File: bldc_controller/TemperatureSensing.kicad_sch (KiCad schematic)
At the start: 9 parts

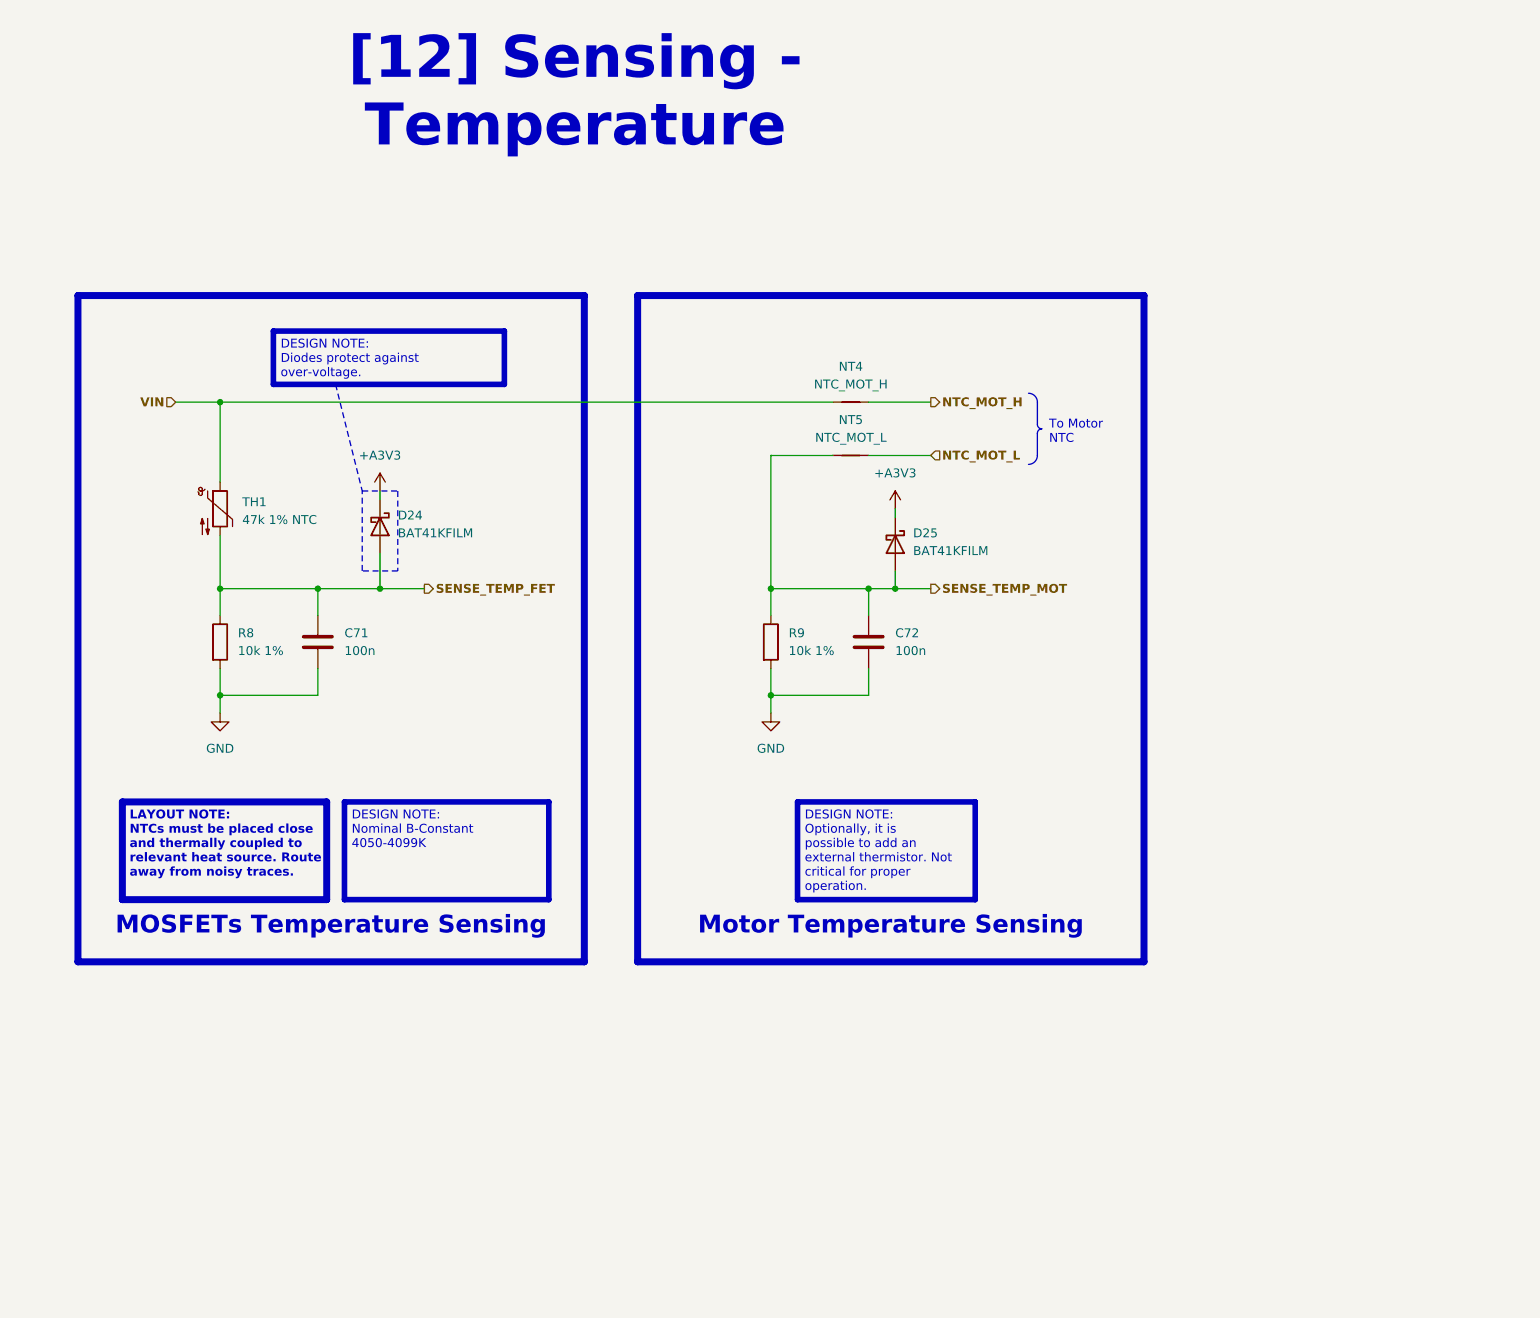
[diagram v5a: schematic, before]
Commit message: Replaced 3v3 buck with WSON package alternative. Will back-annotate components
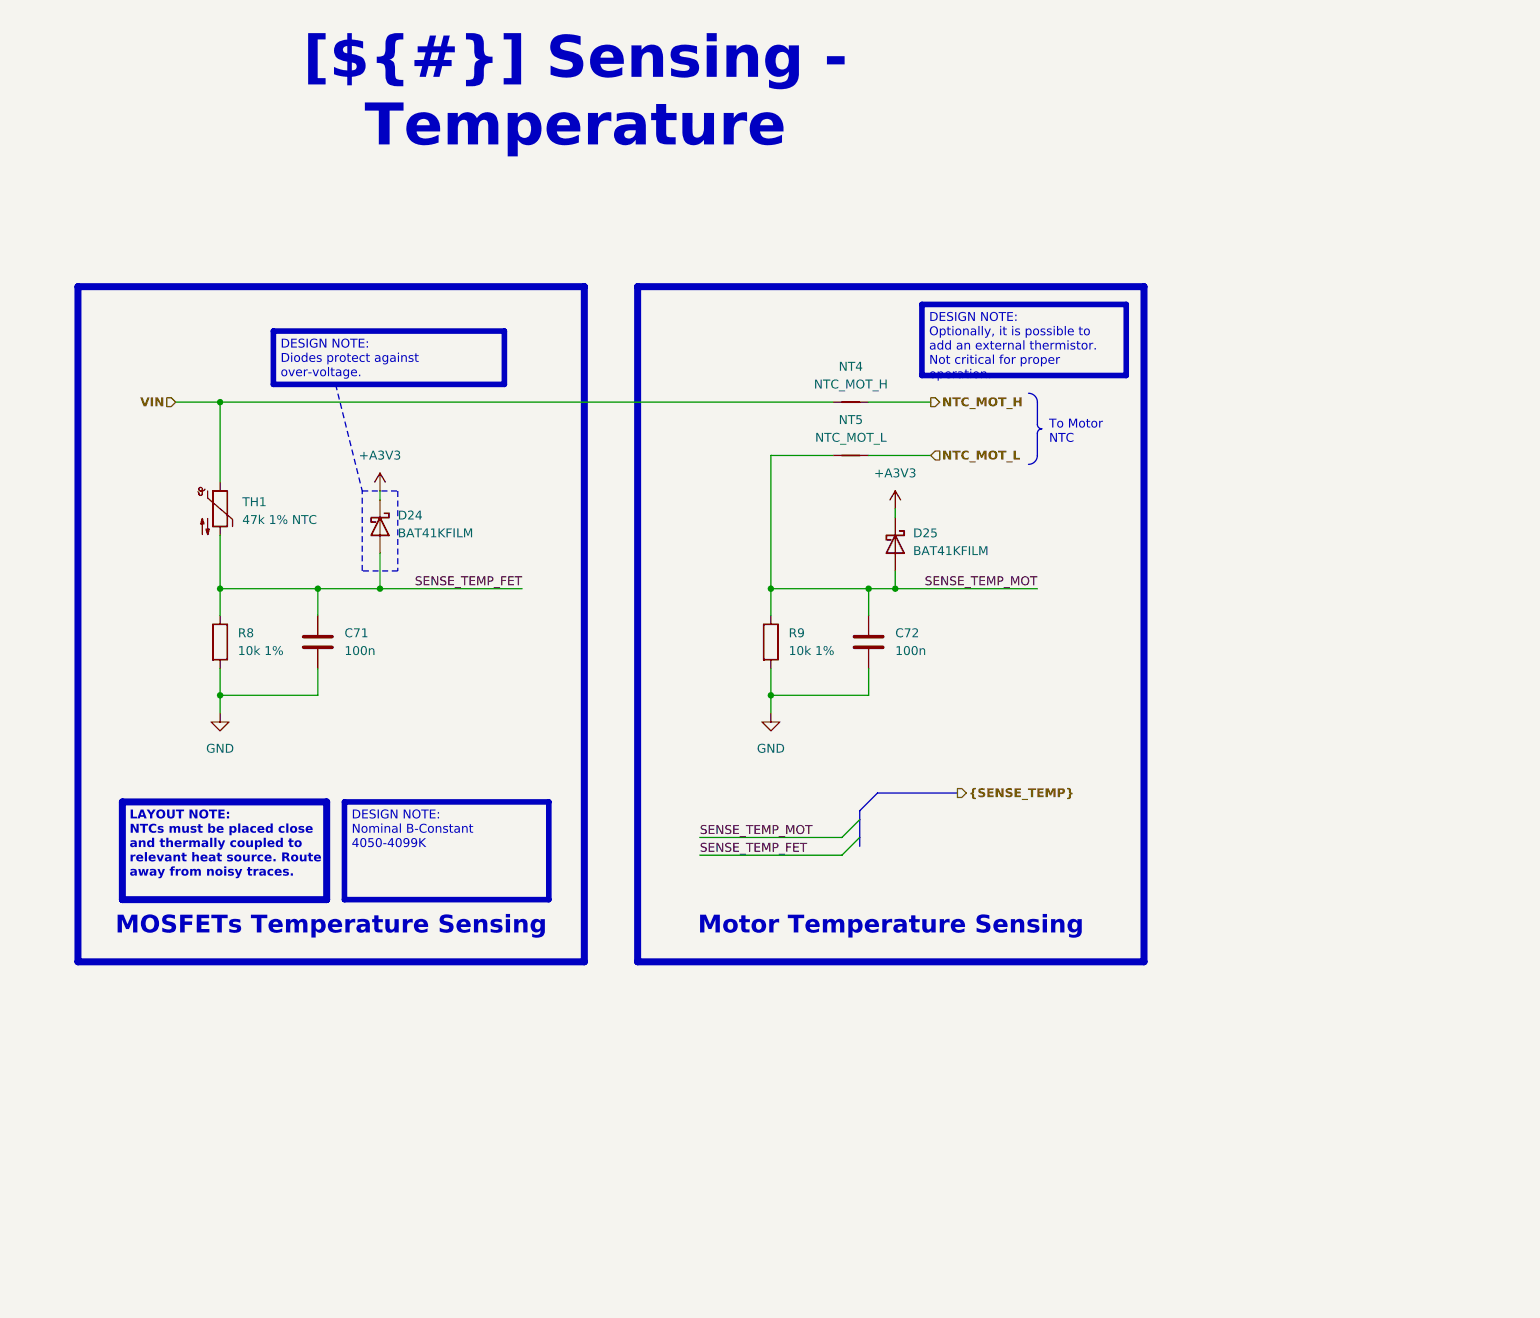
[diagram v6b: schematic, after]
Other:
- company: EPFL Xplore -> ${COMPANY}
- title: Temperature Sensing -> Sensing - Temperature
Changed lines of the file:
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@@
   (paper "A4")
   (title_block
-    (title "Temperature Sensing")
+    (title "Sensing - Temperature")
     (date "2023-10-14")
-    (rev "1.0")
-    (company "EPFL Xplore")
-    (comment 3 "Author: Vincent Nguyen")
+    (rev "${REVISION}")
+    (company "${COMPANY}")
+    (comment 3 "Author: ${AUTHOR}")
   )
   (junction (at 194.31 93.98) (diameter 0) (color 0 0 0 0)
@@
   (junction (at 190.5 93.98) (diameter 0) (color 0 0 0 0)
   )
-  (junction (at 97.79 109.22) (diameter 0) (color 0 0 0 1)
-  )
-  (junction (at 176.53 109.22) (diameter 0) (color 0 0 0 1)
+  (junction (at 97.79 109.22) (diameter 0) (color 0 0 0 0)
+  )
+  (junction (at 176.53 109.22) (diameter 0) (color 0 0 0 0)
   )
   (junction (at 111.76 93.98) (diameter 0) (color 0 0 0 0)
   )
+  (bus_entry (at 186.69 129.54) (size 2.54 -2.54)
+    (stroke (width 0) (type default))
+  )
+  (bus_entry (at 186.69 132.08) (size 2.54 -2.54)
+    (stroke (width 0) (type default))
+  )
   (wire (pts (xy 97.79 67.31) (xy 185.42 67.31))
     (stroke (width 0) (type default))
@@
   )
   (wire (pts (xy 176.53 109.22) (xy 190.5 109.22))
-    (stroke (width 0.381) (type default) (color 0 0 0 1))
+    (stroke (width 0) (type default))
   )
   (wire (pts (xy 120.65 80.01) (xy 120.65 81.28))
@@
   )
   (wire (pts (xy 97.79 109.22) (xy 111.76 109.22))
-    (stroke (width 0.381) (type default) (color 0 0 0 1))
+    (stroke (width 0) (type default))
   )
   (wire (pts (xy 97.79 93.98) (xy 97.79 97.79))
@@
   )
   (wire (pts (xy 97.79 105.41) (xy 97.79 109.22))
-    (stroke (width 0.381) (type default) (color 0 0 0 1))
+    (stroke (width 0) (type default))
   )
   (wire (pts (xy 97.79 111.76) (xy 97.79 109.22))
-    (stroke (width 0.381) (type default) (color 0 0 0 1))
+    (stroke (width 0) (type default))
   )
   (wire (pts (xy 111.76 93.98) (xy 120.65 93.98))
@@
   )
   (wire (pts (xy 190.5 105.41) (xy 190.5 109.22))
-    (stroke (width 0.381) (type default) (color 0 0 0 1))
+    (stroke (width 0) (type default))
   )
   (wire (pts (xy 111.76 93.98) (xy 111.76 97.79))
     (stroke (width 0) (type default))
   )
-  (wire (pts (xy 120.65 93.98) (xy 127 93.98))
+  (bus (pts (xy 191.77 123.19) (xy 203.2 123.19))
+    (stroke (width 0) (type default))
+  )
+  (wire (pts (xy 120.65 93.98) (xy 140.97 93.98))
     (stroke (width 0) (type default))
   )
@@
     (stroke (width 0) (type default))
   )
+  (bus (pts (xy 189.23 127) (xy 189.23 129.54))
+    (stroke (width 0) (type default))
+  )
+  (bus (pts (xy 189.23 129.54) (xy 189.23 130.81))
+    (stroke (width 0) (type default))
+  )
   (wire (pts (xy 194.31 91.44) (xy 194.31 93.98))
     (stroke (width 0) (type default))
@@
     (stroke (width 0) (type default))
   )
+  (bus (pts (xy 189.23 125.73) (xy 191.77 123.19))
+    (stroke (width 0) (type default))
+  )
   (wire (pts (xy 176.53 111.76) (xy 176.53 109.22))
-    (stroke (width 0.381) (type default) (color 0 0 0 1))
+    (stroke (width 0) (type default))
   )
   (wire (pts (xy 190.5 93.98) (xy 190.5 97.79))
@@
   )
   (wire (pts (xy 111.76 105.41) (xy 111.76 109.22))
-    (stroke (width 0.381) (type default) (color 0 0 0 1))
-  )
-  (wire (pts (xy 194.31 93.98) (xy 199.39 93.98))
+    (stroke (width 0) (type default))
+  )
+  (wire (pts (xy 194.31 93.98) (xy 214.63 93.98))
     (stroke (width 0) (type default))
   )
@@
     (stroke (width 0) (type default))
   )
+  (bus (pts (xy 189.23 125.73) (xy 189.23 127))
+    (stroke (width 0) (type default))
+  )
   (wire (pts (xy 176.53 74.93) (xy 176.53 93.98))
     (stroke (width 0) (type default))
   )
   (wire (pts (xy 176.53 105.41) (xy 176.53 109.22))
-    (stroke (width 0.381) (type default) (color 0 0 0 1))
+    (stroke (width 0) (type default))
+  )
+  (wire (pts (xy 166.37 129.54) (xy 186.69 129.54))
+    (stroke (width 0) (type default))
   )
   (wire (pts (xy 91.44 67.31) (xy 97.79 67.31))
+    (stroke (width 0) (type default))
+  )
+  (wire (pts (xy 166.37 132.08) (xy 186.69 132.08))
     (stroke (width 0) (type default))
   )
@@
     (fill (type none))
   )
-  (rectangle (start 77.47 52.07) (end 149.86 147.32)
+  (rectangle (start 77.47 50.8) (end 149.86 147.32)
     (stroke (width 1) (type default) (color 200 200 200 1))
     (fill (type none))
   )
-  (rectangle (start 157.48 52.07) (end 229.87 147.32)
+  (rectangle (start 157.48 50.8) (end 229.87 147.32)
     (stroke (width 1) (type default) (color 200 200 200 1))
     (fill (type none))
@@
     (effects (font (face "Times New Roman") (size 2.54 2.54) (thickness 0.508) bold (color 162 22 34 1)) (justify bottom))
   )
-  (text_box "[12] Sensing - Temperature"
+  (text_box "[${#}] ${TITLE}"
     (at 80.01 16.51 0) (size 137.16 12.7)
     (stroke (width -0.0001) (type default))
@@
   )
   (text_box "DESIGN NOTE:\nOptionally, it is possible to add an external thermistor. Not critical for proper operation."
-    (at 180.34 124.46 0) (size 25.4 13.97)
+    (at 198.12 53.34 0) (size 29.21 10.16)
     (stroke (width 0.8) (type solid) (color 255 165 0 1))
     (fill (type none))
@@
     (effects (font (face "Arial") (size 1.27 1.27) (color 0 0 0 1)) (justify left top))
   )
+  (label "SENSE_TEMP_MOT" (at 214.63 93.98 180) (fields_autoplaced)
+    (effects (font (size 1.27 1.27)) (justify right bottom))
+  )
+  (label "SENSE_TEMP_FET" (at 166.37 132.08 0) (fields_autoplaced)
+    (effects (font (size 1.27 1.27)) (justify left bottom))
+  )
+  (label "SENSE_TEMP_MOT" (at 166.37 129.54 0) (fields_autoplaced)
+    (effects (font (size 1.27 1.27)) (justify left bottom))
+  )
+  (label "SENSE_TEMP_FET" (at 140.97 93.98 180) (fields_autoplaced)
+    (effects (font (size 1.27 1.27)) (justify right bottom))
+  )
   (hierarchical_label "VIN" (shape input) (at 91.44 67.31 180) (fields_autoplaced)
     (effects (font (size 1.27 1.27) bold) (justify right))
@@
     (effects (font (size 1.27 1.27) bold) (justify left))
   )
-  (hierarchical_label "SENSE_TEMP_FET" (shape output) (at 127 93.98 0) (fields_autoplaced)
+  (hierarchical_label "{SENSE_TEMP}" (shape output) (at 203.2 123.19 0) (fields_autoplaced)
     (effects (font (size 1.27 1.27) bold) (justify left))
   )
@@
     (effects (font (size 1.27 1.27) bold) (justify left))
   )
-  (hierarchical_label "SENSE_TEMP_MOT" (shape output) (at 199.39 93.98 0) (fields_autoplaced)
-    (effects (font (size 1.27 1.27) bold) (justify left))
-  )
